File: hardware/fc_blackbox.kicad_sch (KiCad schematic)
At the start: 3 parts

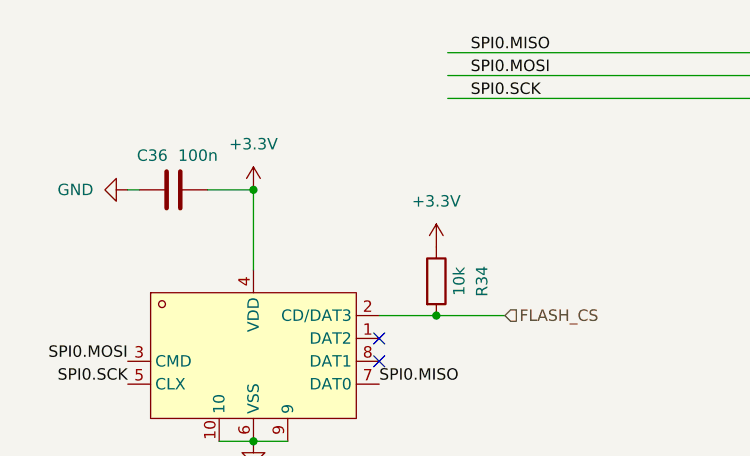
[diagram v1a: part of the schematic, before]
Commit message: OpenAIO: new marker test points TP29 (BUZZER-) and TP30 (+5V) on the Base; lga_apply only excludes the markers it consumed
Co-Authored-By: Claude Fable 5 <noreply@anthropic.com>
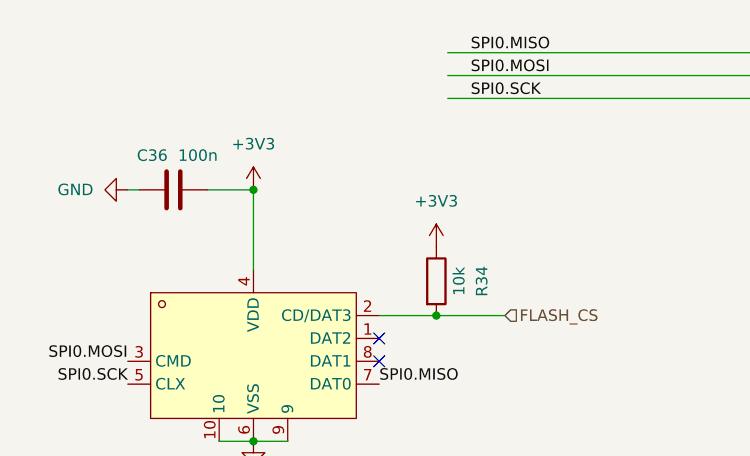
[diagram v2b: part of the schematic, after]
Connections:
- net +3.3V renamed +3V3
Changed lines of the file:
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@@
+	)
+	(junction
+		(at 72.39 78.74)
+		(diameter 0)
+		(color 0 0 0 0)
 	)
 	(junction
 		(at 72.39 50.8)
-		(diameter 0)
-		(color 0 0 0 0)
-	)
-	(junction
-		(at 72.39 78.74)
 		(diameter 0)
 		(color 0 0 0 0)
@@
 			)
 			(justify left)
-		)
-	)
-	(symbol
-		(lib_id "power:+3.3V")
-		(at 72.39 50.8 0)
-		(unit 1)
-		(body_style 1)
-		(exclude_from_sim no)
-		(in_bom yes)
-		(on_board yes)
-		(in_pos_files yes)
-		(dnp no)
-		(fields_autoplaced yes)
-		(property "Reference" "#PWR0103"
-			(at 72.39 54.61 0)
-			(hide yes)
-			(show_name no)
-			(do_not_autoplace no)
-			(effects
-				(font
-					(size 1.27 1.27)
-				)
-			)
-		)
-		(property "Value" "+3.3V"
-			(at 72.39 45.72 0)
-			(show_name no)
-			(do_not_autoplace no)
-			(effects
-				(font
-					(size 1.27 1.27)
-				)
-			)
-		)
-		(property "Footprint" ""
-			(at 72.39 50.8 0)
-			(hide yes)
-			(show_name no)
-			(do_not_autoplace no)
-			(effects
-				(font
-					(size 1.27 1.27)
-				)
-			)
-		)
-		(property "Datasheet" ""
-			(at 72.39 50.8 0)
-			(hide yes)
-			(show_name no)
-			(do_not_autoplace no)
-			(effects
-				(font
-					(size 1.27 1.27)
-				)
-			)
-		)
-		(property "Description" "Power symbol creates a global label with name \"+3.3V\""
-			(at 72.39 50.8 0)
-			(hide yes)
-			(show_name no)
-			(do_not_autoplace no)
-			(effects
-				(font
-					(size 1.27 1.27)
-				)
-			)
-		)
-		(pin "1"
-		)
-		(instances
-			(project "OpenAIO-Base"
-				(path "/fb88b6f9-ee39-4640-a9d4-04a17ceeac64/92d80a6e-4bd9-4df0-920d-da7b8cdc2925"
-					(reference "#PWR0103")
-					(unit 1)
-				)
-			)
 		)
 	)
@@
 	)
 	(symbol
-		(lib_id "power:+3.3V")
-		(at 92.71 57.15 0)
-		(unit 1)
-		(body_style 1)
-		(exclude_from_sim no)
-		(in_bom yes)
-		(on_board yes)
-		(in_pos_files yes)
-		(dnp no)
-		(fields_autoplaced yes)
-		(property "Reference" "#PWR0105"
-			(at 92.71 60.96 0)
-			(hide yes)
-			(show_name no)
-			(do_not_autoplace no)
-			(effects
-				(font
-					(size 1.27 1.27)
-				)
-			)
-		)
-		(property "Value" "+3.3V"
-			(at 92.71 52.07 0)
-			(show_name no)
-			(do_not_autoplace no)
-			(effects
-				(font
-					(size 1.27 1.27)
-				)
-			)
-		)
-		(property "Footprint" ""
-			(at 92.71 57.15 0)
-			(hide yes)
-			(show_name no)
-			(do_not_autoplace no)
-			(effects
-				(font
-					(size 1.27 1.27)
-				)
-			)
-		)
-		(property "Datasheet" ""
-			(at 92.71 57.15 0)
-			(hide yes)
-			(show_name no)
-			(do_not_autoplace no)
-			(effects
-				(font
-					(size 1.27 1.27)
-				)
-			)
-		)
-		(property "Description" "Power symbol creates a global label with name \"+3.3V\""
-			(at 92.71 57.15 0)
-			(hide yes)
-			(show_name no)
-			(do_not_autoplace no)
-			(effects
-				(font
-					(size 1.27 1.27)
-				)
-			)
-		)
-		(pin "1"
-		)
-		(instances
-			(project "OpenAIO-Base"
-				(path "/fb88b6f9-ee39-4640-a9d4-04a17ceeac64/92d80a6e-4bd9-4df0-920d-da7b8cdc2925"
-					(reference "#PWR0105")
-					(unit 1)
-				)
-			)
-		)
-	)
-	(symbol
 		(lib_id "Device:C")
 		(at 63.5 50.8 270)
@@
 					(unit 1)
 				)
+			)
+		)
+	)
+	(symbol
+		(lib_id "power:+3V3")
+		(at 92.71 57.15 0)
+		(unit 1)
+		(body_style 1)
+		(exclude_from_sim no)
+		(in_bom yes)
+		(on_board yes)
+		(in_pos_files yes)
+		(dnp no)
+		(fields_autoplaced yes)
+		(property "Reference" "#PWR0286"
+			(at 92.71 60.96 0)
+			(hide yes)
+			(show_name no)
+			(do_not_autoplace no)
+			(effects
+				(font
+					(size 1.27 1.27)
+				)
+			)
+		)
+		(property "Value" "+3V3"
+			(at 92.71 52.07 0)
+			(show_name no)
+			(do_not_autoplace no)
+			(effects
+				(font
+					(size 1.27 1.27)
+				)
+			)
+		)
+		(property "Footprint" ""
+			(at 92.71 57.15 0)
+			(hide yes)
+			(show_name no)
+			(do_not_autoplace no)
+			(effects
+				(font
+					(size 1.27 1.27)
+				)
+			)
+		)
+		(property "Datasheet" ""
+			(at 92.71 57.15 0)
+			(hide yes)
+			(show_name no)
+			(do_not_autoplace no)
+			(effects
+				(font
+					(size 1.27 1.27)
+				)
+			)
+		)
+		(property "Description" "Power symbol creates a global label with name \"+3V3\""
+			(at 92.71 57.15 0)
+			(hide yes)
+			(show_name no)
+			(do_not_autoplace no)
+			(effects
+				(font
+					(size 1.27 1.27)
+				)
+			)
+		)
+		(pin "1"
+		)
+		(instances
+			(project "OpenAIO-Base"
+				(path "/fb88b6f9-ee39-4640-a9d4-04a17ceeac64/92d80a6e-4bd9-4df0-920d-da7b8cdc2925"
+					(reference "#PWR0286")
+					(unit 1)
+				)
+			)
+		)
+	)
+	(symbol
+		(lib_id "power:+3V3")
+		(at 72.39 50.8 0)
+		(unit 1)
+		(body_style 1)
+		(exclude_from_sim no)
+		(in_bom yes)
+		(on_board yes)
+		(in_pos_files yes)
+		(dnp no)
+		(fields_autoplaced yes)
+		(property "Reference" "#PWR0287"
+			(at 72.39 54.61 0)
+			(hide yes)
+			(show_name no)
+			(do_not_autoplace no)
+			(effects
+				(font
+					(size 1.27 1.27)
+				)
+			)
+		)
+		(property "Value" "+3V3"
+			(at 72.39 45.72 0)
+			(show_name no)
+			(do_not_autoplace no)
+			(effects
+				(font
+					(size 1.27 1.27)
+				)
+			)
+		)
+		(property "Footprint" ""
+			(at 72.39 50.8 0)
+			(hide yes)
+			(show_name no)
+			(do_not_autoplace no)
+			(effects
+				(font
+					(size 1.27 1.27)
+				)
+			)
+		)
+		(property "Datasheet" ""
+			(at 72.39 50.8 0)
+			(hide yes)
+			(show_name no)
+			(do_not_autoplace no)
+			(effects
+				(font
+					(size 1.27 1.27)
+				)
+			)
+		)
+		(property "Description" "Power symbol creates a global label with name \"+3V3\""
+			(at 72.39 50.8 0)
+			(hide yes)
+			(show_name no)
+			(do_not_autoplace no)
+			(effects
+				(font
+					(size 1.27 1.27)
+				)
+			)
+		)
+		(pin "1"
+		)
+		(instances
+			(project "OpenAIO-Base"
+				(path "/fb88b6f9-ee39-4640-a9d4-04a17ceeac64/92d80a6e-4bd9-4df0-920d-da7b8cdc2925"
+					(reference "#PWR0287")
+					(unit 1)
+				)

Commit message: Owner rules: no component silk, pad labels and values, no wordmark text, MPN + maker on every BOM line
The owner rules adopted in PLAN.md (pcb-agent-commons, 2026-10-06), applied
where they are local edits:

- No component silkscreen. J91's reference was the only visible one (Core
  B.Silkscreen, under the LGA) and is hidden. Footprint silk graphics removed
  per instance: Base 234, Core 72. Kept: connector outlines and pin-1 marks
  (USB1, U12 SH-6, Card1, JP1) and the LGA pin-1 marks (J90, J91). Base
  lib_footprint_mismatch warnings 31 -> 40 as a result.
- Solder-pad labels: Core J53 (GND) had none, now "gnd" in the style of J52's
  label. The SH-6 per-pin labels ("10v gnd T0", "R0 gnd R1") become the port
  name "DJI" (connectors: name and pin-1 mark only). Core J48-J51 have no room:
  0.5 mm to J44 above, 0.93 mm to the board edge below. CIRCUIT_REVIEW 8.3
  moves them off the LGA in R2, so their labels go with that move.
- Pad values: all 40 solder-pad symbols said "5V". Each now carries its
  function (5V, GND, LED, BUZ+/BUZ-, 10V, 4V5, CAM, VTX, SCL, SDA, TX0/RX0,
  TX1/RX1, PIO_TX0/PIO_RX0; off-board J19 ADC2, J22 GND, J46/J47 NC).
- No "Drone" text: the "OpenDrone" wordmark on Core F.Silkscreen (9 filled
  polygons in two groups) is removed; a TODO for the incutec wordmark from the
  brand repo sits on User.Comments (not fabricated). No other such text on any
  copper, mask or silk layer of either board.
- BOM: lines missing manufacturer or MPN 41 -> 1. MPNs come from
  PARTS-USED.md by LCSC number. Manufacturers come from the catalogue symbol,
  this design's spelling for the same MPN family, or the committed datasheet
  (NSIC, Sofng, Jiangsu Changjing, Hirose). Still open: Rsense2
  ASR-S-3-0.2F (C695806), whose manufacturer nothing in the catalogue states.
  U24 (board outline) and TP9 (BOOT solder pad) are not parts: excluded from
  BOM and position files.
- 0201 default / minimal capacitance: respected in the circuit commit (C26
  stays 0201; no belt-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
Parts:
- Card1: MPN (none) -> TF-021B-H265; Manufacturer (none) -> SOFNG
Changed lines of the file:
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@@
+			)
+		)
+		(property "MPN" "TF-021B-H265"
+			(at 72.39 57.15 0)
+			(hide yes)
+			(show_name no)
+			(do_not_autoplace no)
+			(effects
+				(font
+					(size 1.27 1.27)
+				)
+				(justify left)
+			)
+		)
+		(property "Manufacturer" "SOFNG"
+			(at 72.39 57.15 0)
+			(hide yes)
+			(show_name no)
+			(do_not_autoplace no)
+			(effects
+				(font
+					(size 1.27 1.27)
+				)
+				(justify left)
 			)
 		)
@@
 		)
 	)
-	(embedded_fonts no)
 )

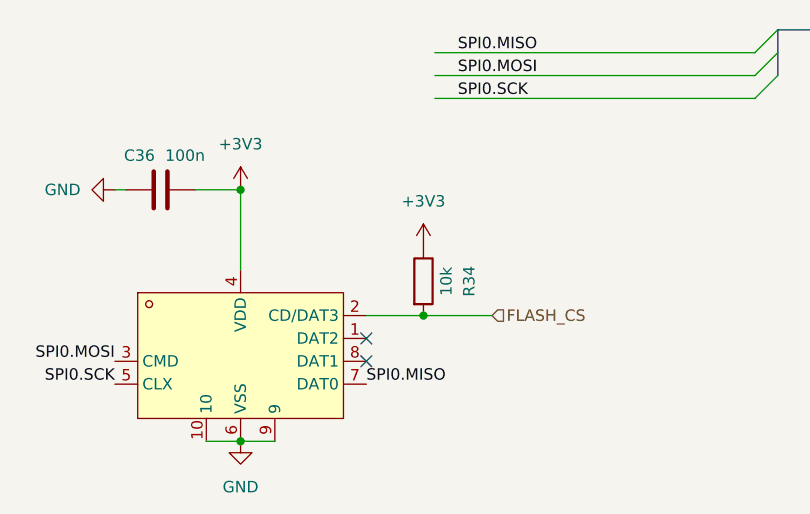
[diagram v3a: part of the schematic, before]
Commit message: One board: merge Base and Core onto the OpenAIO-Whoop 8L HDI stackup
- hardware/OpenAIO.kicad_pcb: the routed Base and Core layouts of 8fa8d7b
  side by side in one board, all routing kept (Core promoted to 8 layers
  before the append so no Base layer was dropped). J90/J91 LGA deleted;
  their 46 nets are now direct links (51 unconnected, listed in
  research/ROUTING.md). Stackup and board setup from OpenAIO-Whoop:
  8L HDI 1+6+1, 0.997 mm, 1 oz all layers, microvia 0.25/0.10,
  buried 0.33/0.15. Base DRC severities and exclusions kept.
- hardware/OpenAIO.kicad_dru: canonical block, Whoop HDI via rules,
  Base/Core rules that still apply; LGA, 2 oz and 1.6 mm via rules gone.
- Schematic: core_interface sheet removed; DPS368 baro U28 on I2C0;
  review fixes (U3 HF cap C116, RP2354 caps C117/C118, buzzer flyback D10,
  SD card on +3.3V, D9 on +4v5, FLASH_CS -> SD_CS, PWR_FLAGs, U7 pin
  names, ESC cap pin types, L4 LCSC). ERC 32 -> 0 errors.
- Libraries project-local: every footprint, 3D model and symbol in lib;
  OPENDRONE_LIB aliases removed from the lib tables.
- Two-board projects, multiboard config and LGA tools removed; Whoop
  board tools added in hardware/tools.
- Docs: README, AGENTS.md, research/ROUTING.md (hand-over),
  SCHEMATIC-REVIEW-2026-10-15.md, Betaflight target baro.

DRC: 38 errors (25 dangling LGA escape vias, 13 Core leftovers listed),
51 unconnected (the Base-Core links), 0 net or value parity issues.

Co-Authored-By: Claude Opus 5.5 <noreply@anthropic.com>
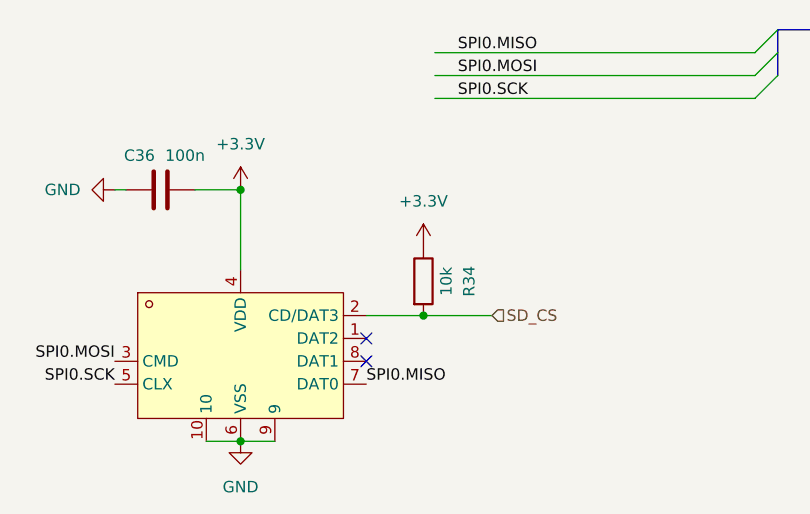
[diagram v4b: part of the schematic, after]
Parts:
- C36: footprint Capacitor_SMD:C_0201_0603Metric -> lib:C_0201_0603Metric
- R34: footprint Resistor_SMD:R_0201_0603Metric -> lib:R_0201_0603Metric
- renumbered Card1 to Card2
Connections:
- net +3V3 renamed +3.3V
- net FLASH_CS renamed SD_CS
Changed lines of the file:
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@@
 		)
 	)
-	(hierarchical_label "FLASH_CS"
+	(hierarchical_label "SD_CS"
 		(shape input)
 		(at 100.33 64.77 0)
@@
 			)
 		)
-		(property "Footprint" "Resistor_SMD:R_0201_0603Metric"
+		(property "Footprint" "lib:R_0201_0603Metric"
 			(at 90.932 60.96 90)
 			(hide yes)
@@
 		(in_pos_files yes)
 		(dnp no)
-		(property "Reference" "Card1"
+		(property "Reference" "Card2"
 			(at 72.39 77.47 0)
 			(hide yes)
@@
 		)
 		(instances
-			(project "BLACKBOX"
+			(project ""
 				(path "/7bc7eb1e-1a25-4797-98f3-e49fc3746593"
 					(reference "Card2")
@@
 			)
 		)
-		(property "Footprint" "Capacitor_SMD:C_0201_0603Metric"
+		(property "Footprint" "lib:C_0201_0603Metric"
 			(at 59.69 51.7652 0)
 			(hide yes)
@@
 			)
 		)
-		(property "Value" "+3V3"
+		(property "Value" "+3.3V"
 			(at 92.71 52.07 0)
 			(show_name no)
@@
 			)
 		)
-		(property "Value" "+3V3"
+		(property "Value" "+3.3V"
 			(at 72.39 45.72 0)
 			(show_name no)

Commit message: One board from the owner's 2026-08-22 Base and Core, BMP580 baro (#26)
The board is rebuilt from d81e559 (the hand-routed Base recovered from KiCad
local history and the hand-routed Core of 1fe3d21) plus the always-on +10V of
9aba717, instead of the agent-reworked 8fa8d7b. Both layouts sit side by side
in hardware/OpenAIO.kicad_pcb with all routing kept (2513 tracks, 1577 vias),
on the OpenAIO-Whoop 8L HDI stackup.

- Schematic: Core_Interface (J90/J91 LGA) removed; U26 BMP580 + C107/C108 on
  I2C0 at 0x47 (Betaflight BMP5xx default). Netlist otherwise identical to
  9aba717; ERC 31 errors, the 9aba717 baseline.
- Board: Base netclasses and severities; rule area "Core layout" keeps the
  Core's 0.09 line standard. DRC: 3 errors (USB1 peg), 37 unconnected (links).
- lib.pretty footprints replaced by the board instances; BMP580 imported with
  easyeda2kicad (LCSC C22391138).
- Not carried from 8fa8d7b: TXU0101 LED-strip buffer, +3V3_ESC, SWD pads,
  DFM edits; firmware ISSUES I2/I3 reopened.
- Docs: README pinout re-measured, AGENTS.md, research/ROUTING.md, Betaflight
  target USE_BARO_BMP580.

Co-authored-by: Stan <stan@openaio.local>
Co-authored-by: Claude Opus 5.5 <noreply@anthropic.com>
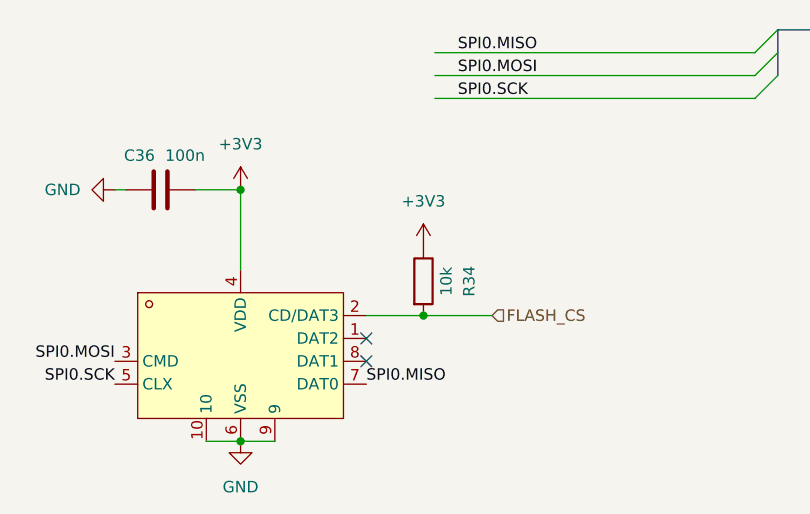
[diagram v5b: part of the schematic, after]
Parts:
- Card2: MPN TF-021B-H265 -> (none); Manufacturer SOFNG -> (none)
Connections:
- net +3.3V renamed +3V3
- net SD_CS renamed FLASH_CS
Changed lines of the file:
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@@
 		)
 	)
-	(hierarchical_label "SD_CS"
+	(hierarchical_label "FLASH_CS"
 		(shape input)
 		(at 100.33 64.77 0)
@@
 		(property "LCSC" "C498185"
 			(at 74.93 73.6599 0)
-			(hide yes)
-			(show_name no)
-			(do_not_autoplace no)
-			(effects
-				(font
-					(size 1.27 1.27)
-				)
-				(justify left)
-			)
-		)
-		(property "MPN" "TF-021B-H265"
-			(at 72.39 57.15 0)
-			(hide yes)
-			(show_name no)
-			(do_not_autoplace no)
-			(effects
-				(font
-					(size 1.27 1.27)
-				)
-				(justify left)
-			)
-		)
-		(property "Manufacturer" "SOFNG"
-			(at 72.39 57.15 0)
 			(hide yes)
 			(show_name no)
@@
 			)
 		)
-		(property "Value" "+3.3V"
+		(property "Value" "+3V3"
 			(at 92.71 52.07 0)
 			(show_name no)
@@
 			)
 		)
-		(property "Value" "+3.3V"
+		(property "Value" "+3V3"
 			(at 72.39 45.72 0)
 			(show_name no)
